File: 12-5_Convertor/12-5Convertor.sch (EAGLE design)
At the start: 14 parts, among them U1 LM2678

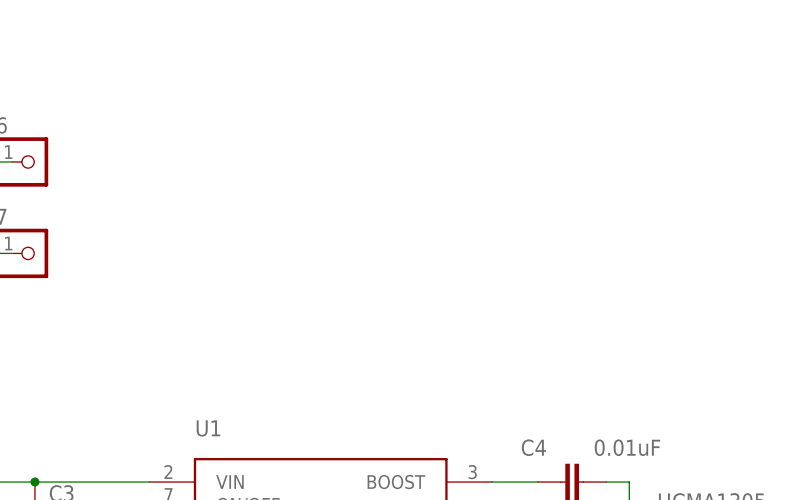
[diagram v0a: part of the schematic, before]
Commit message: Update the buck regulator.
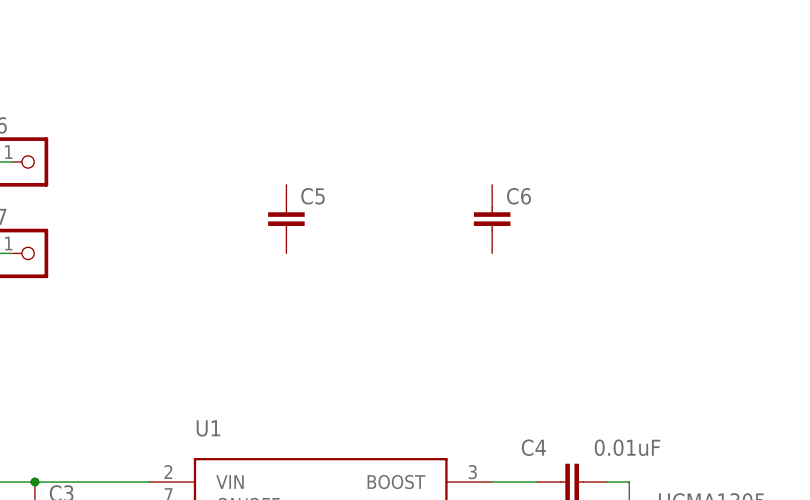
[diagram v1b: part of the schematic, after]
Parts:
- added C5, C6: (no value), eagle-ltspice:CC0603
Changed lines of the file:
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@@
 <?xml version="1.0" encoding="utf-8"?>
 <!DOCTYPE eagle SYSTEM "eagle.dtd">
-<eagle version="7.3.0">
+<eagle version="7.4.0">
 <drawing>
 <settings>
@@
 <part name="U$2" library="DiscreteComponents" deviceset="HCMA1305" device=""/>
 <part name="C2" library="PowerComponents" deviceset="C-ALUMINUM(47UF)" device=""/>
+<part name="C5" library="eagle-ltspice" deviceset="C" device="C0603"/>
+<part name="C6" library="eagle-ltspice" deviceset="C" device="C0603"/>
 </parts>
 <sheets>
@@
 <instance part="U$2" gate="G$1" x="96.52" y="73.66" rot="R90"/>
 <instance part="C2" gate="G$1" x="7.62" y="76.2"/>
+<instance part="C5" gate="G$1" x="48.26" y="109.22"/>
+<instance part="C6" gate="G$1" x="71.12" y="109.22"/>
 </instances>
 <busses>

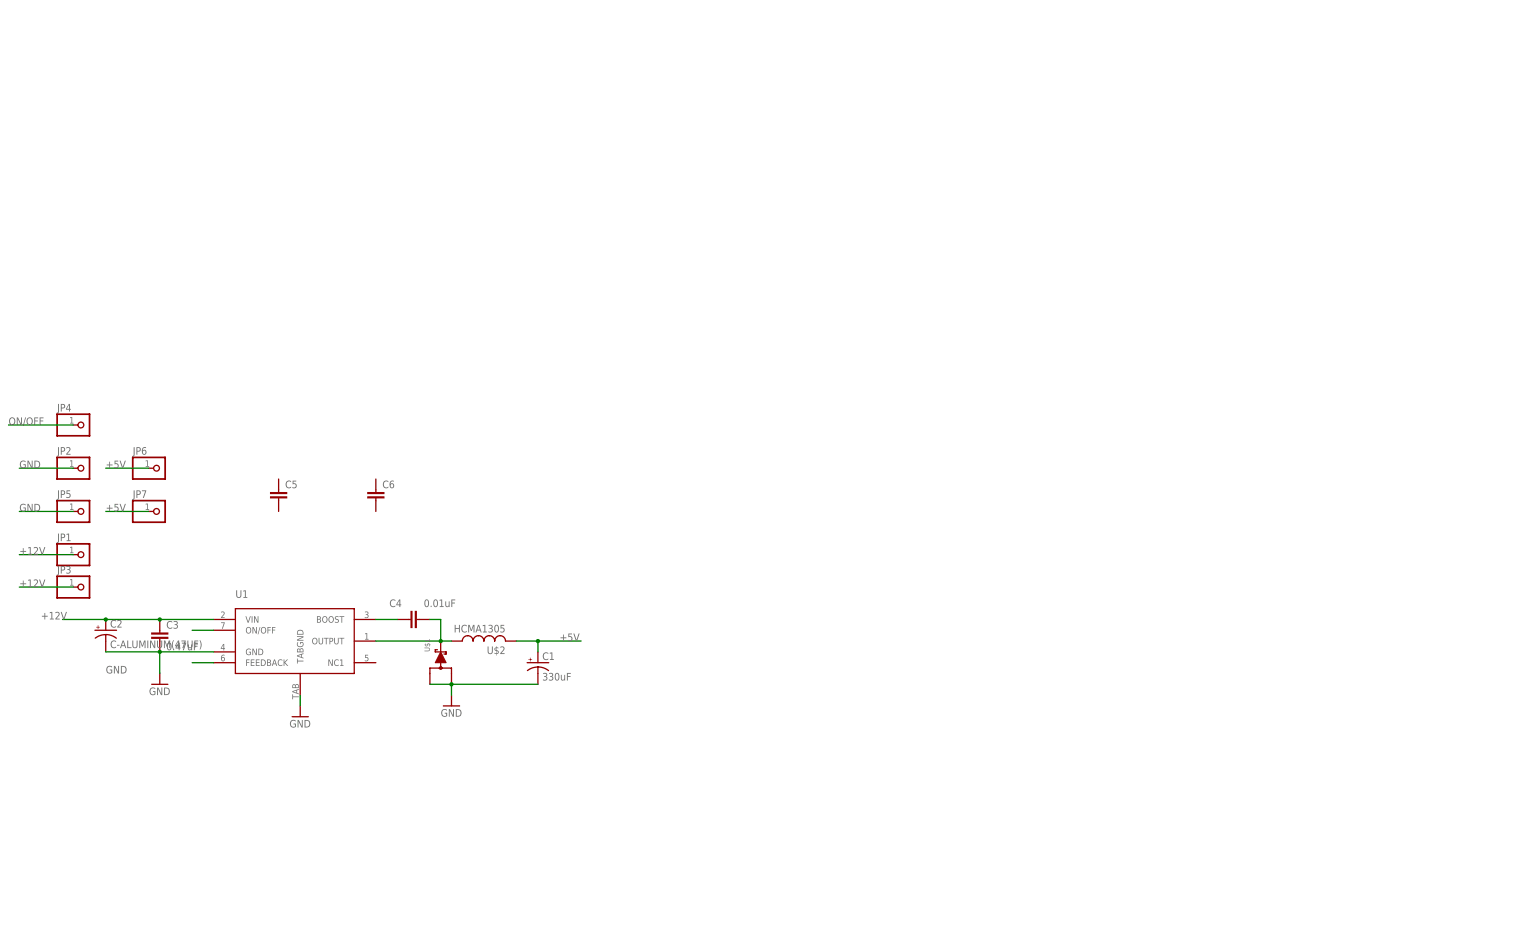
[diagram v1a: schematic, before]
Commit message: Fixed labels. Added linear regulator and current sensor
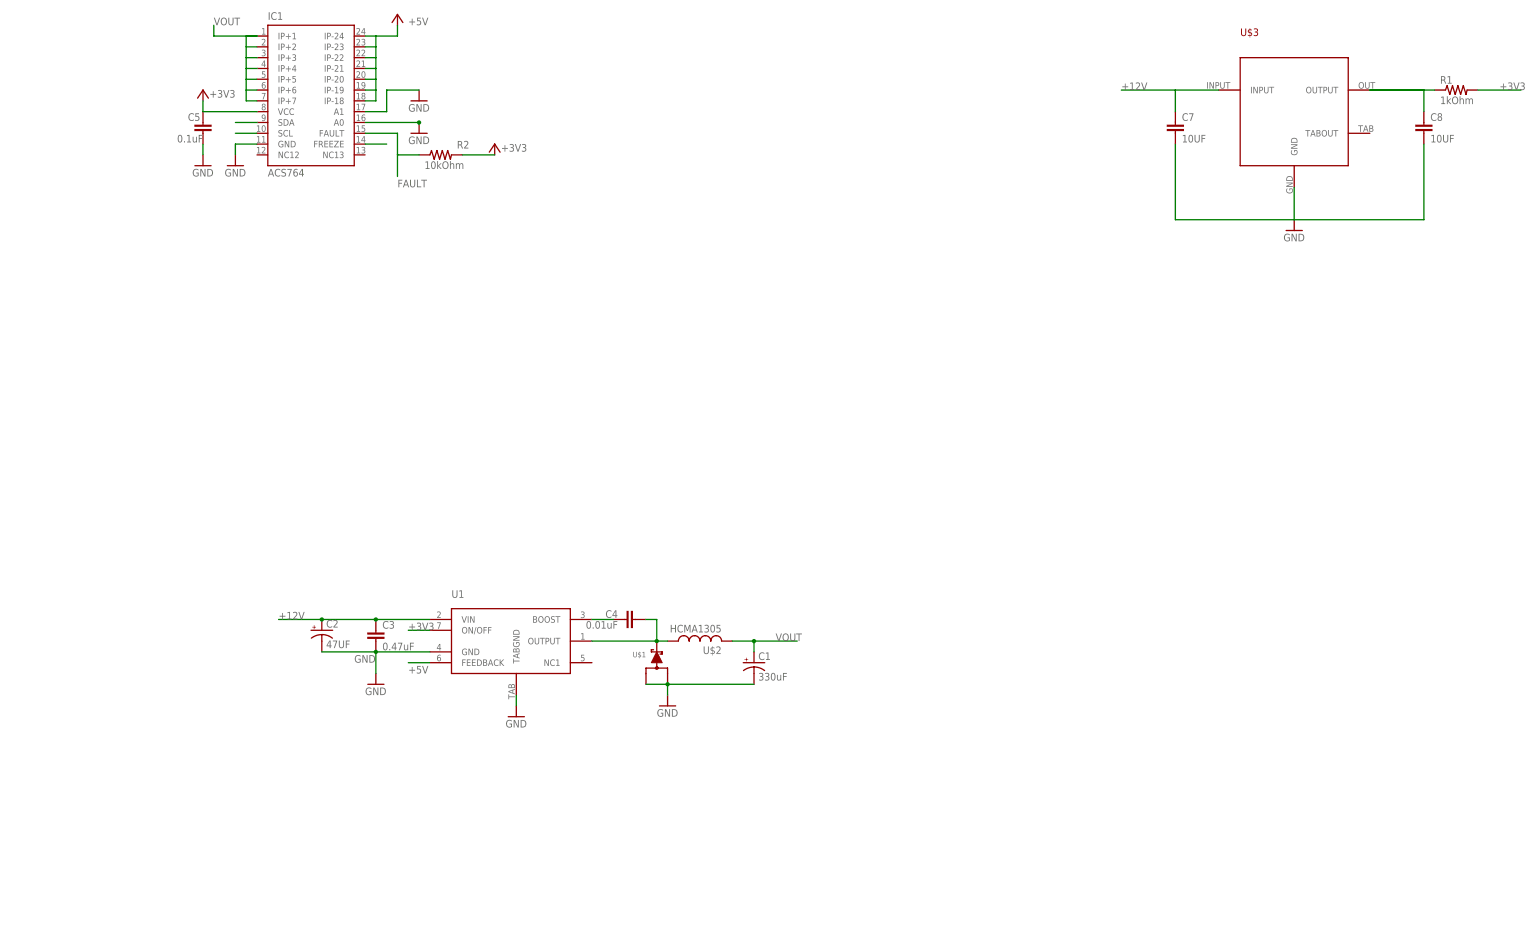
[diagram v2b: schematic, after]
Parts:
- removed C6: (no value), eagle-ltspice:CC0603
- removed JP1, JP2, JP3, JP4, JP5, JP6, JP7: (no value), pinhead:PINHD-1X1
- added C7, C8: 10UF, SparkFun-Passives:CAP0603-CAP
- added IC1: ACS764, ACS764:ACS764
- added R1: 1kOhm, DiscreteComponents:R-US_R0603
- added R2: 10kOhm, DiscreteComponents:R-US_R0603
- added U$3: NCP1117, PowerComponents:NCP1117
- C2: value C-ALUMINUM(47UF) -> 47UF
- C5: value (none) -> 0.1uF
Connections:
- removed net ON/OFF: JP4.1, U1.ON/OFF
- new net +3V3: C5.1, IC1.VCC, R1.2, R2.2, U1.ON/OFF
- new net FAULT: IC1.FAULT, R2.1
- new net N$1: C8.1, R1.1, U$3.OUTPUT
- new net N$10: IC1.FREEZE
- new net N$11: IC1.SDA
- new net N$12: IC1.SCL
- new net VOUT: C1.+, IC1.IP+1, IC1.IP+2, IC1.IP+3, IC1.IP+4, IC1.IP+5, IC1.IP+6, IC1.IP+7, U$2.2
- net +12V: now also C7.1, U$3.INPUT; no longer JP1.1, JP3.1
- net +5V: now also IC1.IP-18, IC1.IP-19, IC1.IP-20, IC1.IP-21, IC1.IP-22, IC1.IP-23, IC1.IP-24; no longer C1.+, JP6.1, JP7.1, U$2.2
- net GND: now also C5.2, C7.2, C8.2, IC1.A0, IC1.A1, IC1.GND, U$3.GND; no longer JP2.1, JP5.1
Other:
- moved on the sheet: C1, C2, C3, C4, C5, U$1, U$2, U1

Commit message: Cleaned up the buck regulator schematic
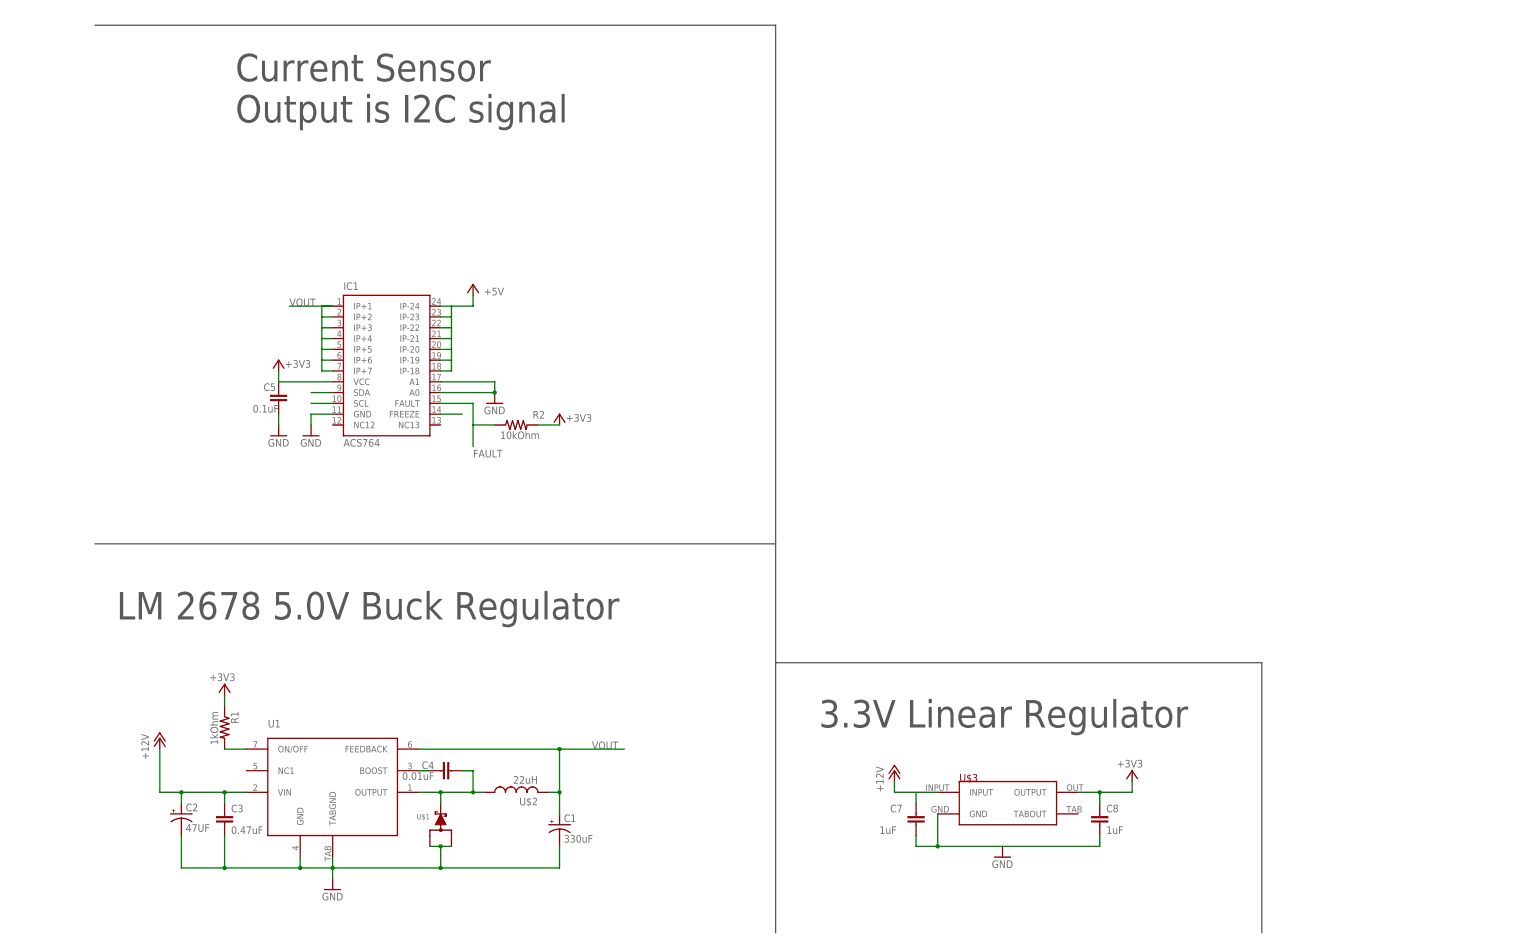
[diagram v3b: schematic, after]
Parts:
- C7, C8: value 10UF -> 1uF
- U$2: value HCMA1305 -> 22uH
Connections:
- removed net N$1: C8.1, R1.1, U$3.OUTPUT
- new net N$5: R1.2, U1.ON/OFF
- net +3V3: now also C8.1, R1.1, U$3.OUTPUT; no longer R1.2, U1.ON/OFF
- net +5V: no longer U1.FEEDBACK
- net VOUT: now also U1.FEEDBACK
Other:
- note added: "3.3V Linear Regulator"
- note added: "Current Sensor Output is I2C signal"
- note added: "LM 2678 5.0V Buck Regulator"
- moved on the sheet: C1, C2, C3, C4, C5, C7, C8, IC1, R1, R2, U$1, U$2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

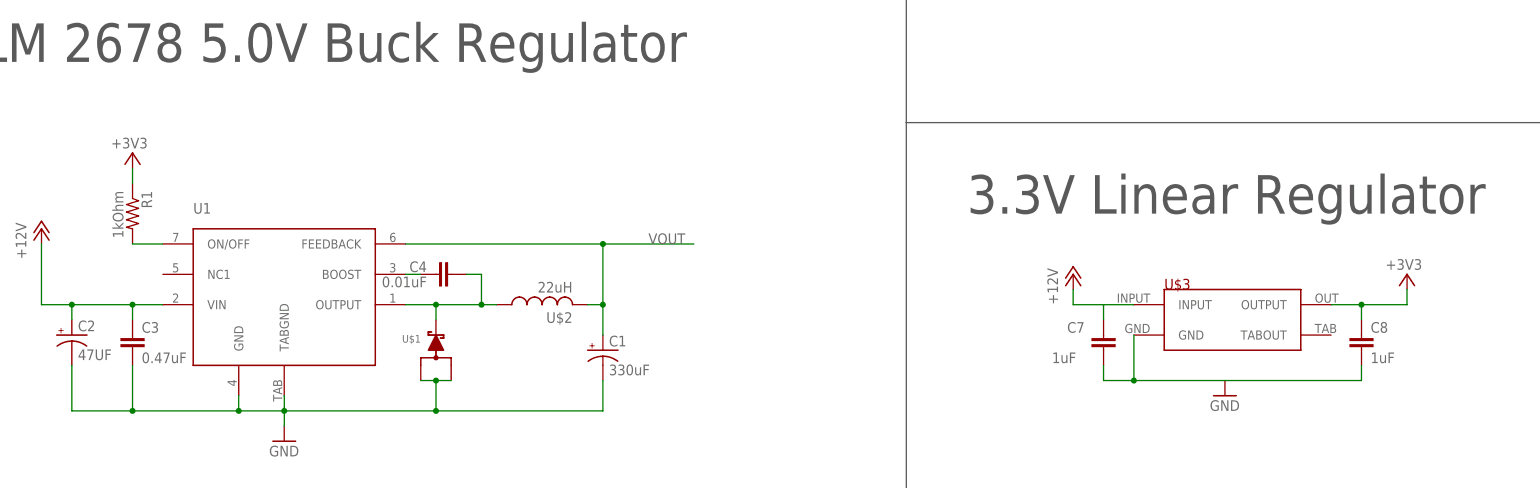
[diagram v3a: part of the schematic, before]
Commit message: Updated the power conversion board
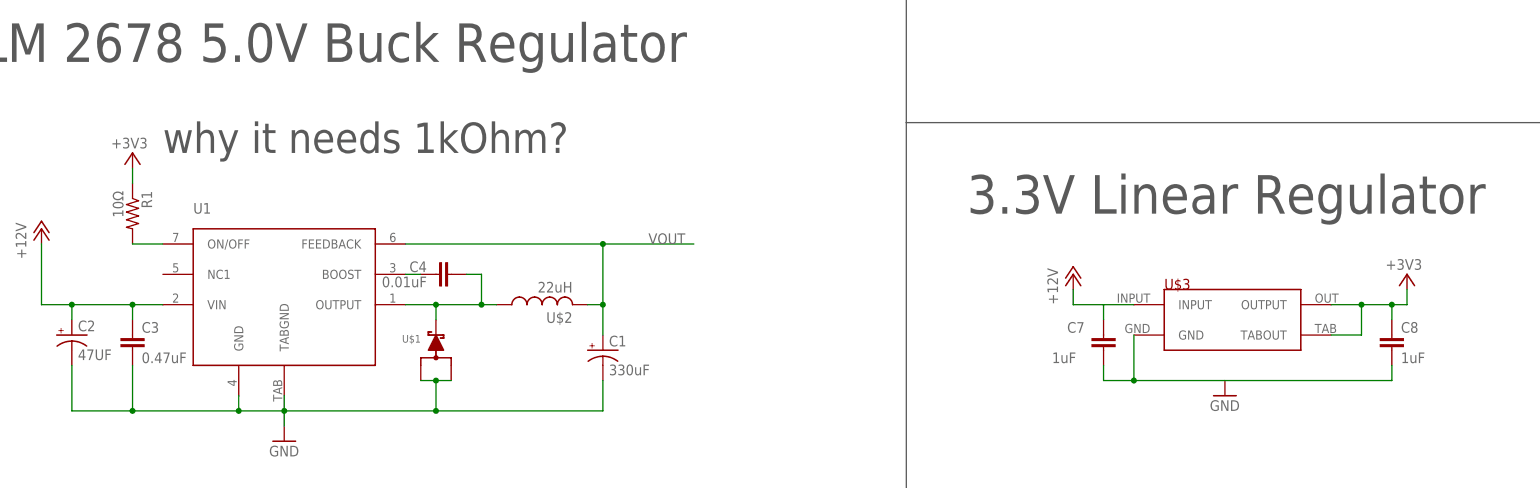
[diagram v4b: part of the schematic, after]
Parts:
- R1: value 1kOhm -> 10Ω
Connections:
- net +3V3: now also U$3.TABOUT
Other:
- note added: "why it needs 1kOhm?"
- moved on the sheet: C8
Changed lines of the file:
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@@
 <?xml version="1.0" encoding="utf-8"?>
 <!DOCTYPE eagle SYSTEM "eagle.dtd">
-<eagle version="7.3.0">
+<eagle version="7.4.0">
 <drawing>
 <settings>
@@
 <part name="C7" library="SparkFun-Passives" deviceset="CAP" device="0603-CAP" value="1uF"/>
 <part name="C8" library="SparkFun-Passives" deviceset="CAP" device="0603-CAP" value="1uF"/>
-<part name="R1" library="DiscreteComponents" deviceset="R-US_" device="R0603" value="1kOhm"/>
+<part name="R1" library="DiscreteComponents" deviceset="R-US_" device="R0603" value="10Ω"/>
 <part name="IC1" library="ACS764" deviceset="ACS764" device=""/>
 <part name="GND3" library="SparkFun-Aesthetics" deviceset="GND" device=""/>
@@
 <text x="38.1" y="195.58" size="6.4516" layer="97">Current Sensor
 Output is I2C signal</text>
+<text x="40.64" y="63.5" size="5.08" layer="97">why it needs 1kOhm?</text>
 </plain>
 <instances>
@@
 <attribute name="VALUE" x="189.484" y="28.321" size="1.778" layer="96"/>
 </instance>
-<instance part="C8" gate="G$1" x="241.3" y="30.48" smashed="yes">
-<attribute name="NAME" x="242.824" y="33.401" size="1.778" layer="95"/>
-<attribute name="VALUE" x="242.824" y="28.321" size="1.778" layer="96"/>
+<instance part="C8" gate="G$1" x="246.38" y="30.48" smashed="yes">
+<attribute name="NAME" x="247.904" y="33.401" size="1.778" layer="95"/>
+<attribute name="VALUE" x="247.904" y="28.321" size="1.778" layer="96"/>
 </instance>
 <instance part="R1" gate="G$1" x="35.56" y="53.34" rot="R270"/>
@@
 <pinref part="C8" gate="G$1" pin="2"/>
 <wire x1="203.2" y1="25.4" x2="218.44" y2="25.4" width="0.1524" layer="91"/>
-<wire x1="218.44" y1="25.4" x2="241.3" y2="25.4" width="0.1524" layer="91"/>
-<wire x1="241.3" y1="25.4" x2="241.3" y2="27.94" width="0.1524" layer="91"/>
+<wire x1="218.44" y1="25.4" x2="246.38" y2="25.4" width="0.1524" layer="91"/>
+<wire x1="246.38" y1="25.4" x2="246.38" y2="27.94" width="0.1524" layer="91"/>
 <pinref part="U$3" gate="G$1" pin="GND"/>
 <wire x1="203.2" y1="33.02" x2="203.2" y2="25.4" width="0.1524" layer="91"/>
@@
 <pinref part="C8" gate="G$1" pin="1"/>
 <wire x1="236.22" y1="38.1" x2="241.3" y2="38.1" width="0.1524" layer="91"/>
-<wire x1="241.3" y1="38.1" x2="241.3" y2="35.56" width="0.1524" layer="91"/>
-<wire x1="241.3" y1="38.1" x2="248.92" y2="38.1" width="0.1524" layer="91"/>
-<junction x="241.3" y="38.1"/>
+<wire x1="241.3" y1="38.1" x2="246.38" y2="38.1" width="0.1524" layer="91"/>
+<wire x1="246.38" y1="38.1" x2="246.38" y2="35.56" width="0.1524" layer="91"/>
+<wire x1="246.38" y1="38.1" x2="248.92" y2="38.1" width="0.1524" layer="91"/>
+<junction x="246.38" y="38.1"/>
 <pinref part="+3V4" gate="G$1" pin="+3V3"/>
 <wire x1="248.92" y1="38.1" x2="248.92" y2="40.64" width="0.1524" layer="91"/>
-</segment>
-</net>
+<pinref part="U$3" gate="G$1" pin="TABOUT"/>
+<wire x1="236.22" y1="33.02" x2="241.3" y2="33.02" width="0.1524" layer="91"/>
+<wire x1="241.3" y1="33.02" x2="241.3" y2="38.1" width="0.1524" layer="91"/>
+<junction x="241.3" y="38.1"/>
+</segment>
+</net>
